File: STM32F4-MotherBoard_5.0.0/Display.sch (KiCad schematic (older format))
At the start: 4 parts

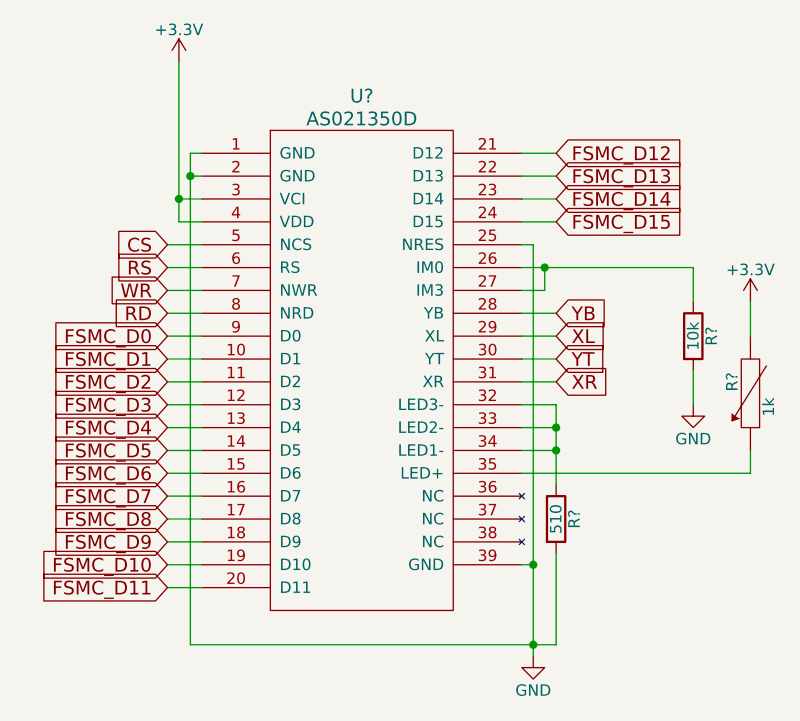
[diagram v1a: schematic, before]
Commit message: SDとCANの追加とラベルミス修正
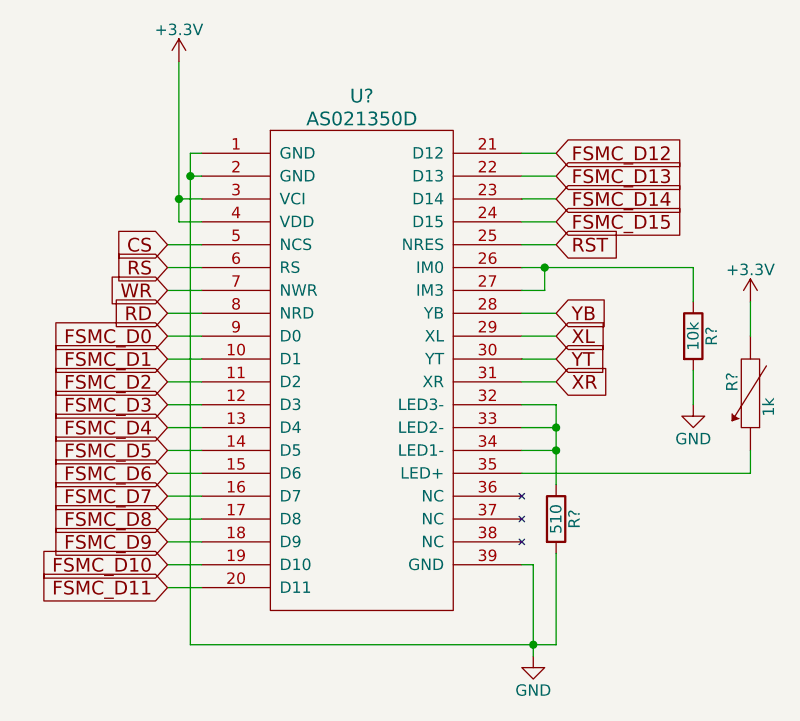
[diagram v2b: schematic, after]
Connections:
- net GND: no longer U?.25 (NRES)
- new net RST: U?.25 (NRES)
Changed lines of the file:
@@
 $Descr A4 11693 8268
 encoding utf-8
-Sheet 7 10
+Sheet 7 11
 Title ""
 Date ""
@@
 Wire Wire Line
 	6300 4750 6350 4750
-Wire Wire Line
-	6350 3350 6350 5150
 $Comp
 L R R?
@@
 Wire Wire Line
 	6300 3950 6450 3950
-Wire Wire Line
-	6300 3350 6350 3350
-Connection ~ 6350 4750
 Wire Wire Line
 	6300 3450 7050 3450
@@
 Text GLabel 4750 3350 0    60   Input ~ 0
 CS
+Wire Wire Line
+	6350 4750 6350 5150
+Text GLabel 6450 3350 2    60   Input ~ 0
+RST
+Wire Wire Line
+	6450 3350 6300 3350
 $EndSCHEMATC

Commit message: 回路図終わり
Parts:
- gave numbers to parts that had none: 4
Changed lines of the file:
@@
 $Descr A4 11693 8268
 encoding utf-8
-Sheet 7 11
+Sheet 7 12
 Title ""
 Date ""
@@
 $EndDescr
 $Comp
-L AS021350D U?
+L AS021350D U6
 U 1 1 589F41CD
 P 5600 2850
-F 0 "U?" H 5600 3000 60  0000 C CNN
+F 0 "U6" H 5600 3000 60  0000 C CNN
 F 1 "AS021350D" H 5600 2900 60  0000 C CNN
 F 2 "" H 5600 2850 60  0000 C CNN
@@
 $EndComp
 $Comp
-L +3.3V #PWR?
+L +3.3V #PWR059
 U 1 1 589F41F4
 P 4800 2550
-F 0 "#PWR?" H 4800 2400 50  0001 C CNN
+F 0 "#PWR059" H 4800 2400 50  0001 C CNN
 F 1 "+3.3V" H 4800 2690 50  0000 C CNN
 F 2 "" H 4800 2550 50  0000 C CNN
@@
 	6300 4750 6350 4750
 $Comp
-L R R?
+L R R31
 U 1 1 589F424B
 P 6450 4550
-F 0 "R?" V 6530 4550 50  0000 C CNN
+F 0 "R31" V 6530 4550 50  0000 C CNN
 F 1 "510" V 6450 4550 50  0000 C CNN
 F 2 "" V 6380 4550 50  0000 C CNN
@@
 Connection ~ 6350 5100
 $Comp
-L GND #PWR?
+L GND #PWR060
 U 1 1 589F4284
 P 6350 5150
-F 0 "#PWR?" H 6350 4900 50  0001 C CNN
+F 0 "#PWR060" H 6350 4900 50  0001 C CNN
 F 1 "GND" H 6350 5000 50  0000 C CNN
 F 2 "" H 6350 5150 50  0000 C CNN
@@
 	7300 4350 7300 4250
 $Comp
-L RVAR R?
+L RVAR R33
 U 1 1 589F433B
 P 7300 4000
-F 0 "R?" V 7380 3950 50  0000 C CNN
+F 0 "R33" V 7380 3950 50  0000 C CNN
 F 1 "1k" V 7220 4060 50  0000 C CNN
 F 2 "" H 7300 4000 50  0000 C CNN
@@
 	7300 3750 7300 3600
 $Comp
-L +3.3V #PWR?
+L +3.3V #PWR061
 U 1 1 589F43A6
 P 7300 3600
-F 0 "#PWR?" H 7300 3450 50  0001 C CNN
+F 0 "#PWR061" H 7300 3450 50  0001 C CNN
 F 1 "+3.3V" H 7300 3740 50  0000 C CNN
 F 2 "" H 7300 3600 50  0000 C CNN
@@
 Connection ~ 6400 3450
 $Comp
-L R R?
+L R R32
 U 1 1 589F454D
 P 7050 3750
-F 0 "R?" V 7130 3750 50  0000 C CNN
+F 0 "R32" V 7130 3750 50  0000 C CNN
 F 1 "10k" V 7050 3750 50  0000 C CNN
 F 2 "" V 6980 3750 50  0000 C CNN
@@
 $EndComp
 $Comp
-L GND #PWR?
+L GND #PWR062
 U 1 1 589F457E
 P 7050 4050
-F 0 "#PWR?" H 7050 3800 50  0001 C CNN
+F 0 "#PWR062" H 7050 3800 50  0001 C CNN
 F 1 "GND" H 7050 3900 50  0000 C CNN
 F 2 "" H 7050 4050 50  0000 C CNN

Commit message: 部品名変更
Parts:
- R31, R32, R33: footprint (none) -> robocon_pcb:SM0603_EXP0.5mm
- U6: footprint (none) -> mylib:ASO21350D
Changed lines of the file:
@@
 EESchema Schematic File Version 2
+LIBS:STM32F4-MotherBoard_5.0.0-rescue
 LIBS:power
 LIBS:device
@@
 F 0 "U6" H 5600 3000 60  0000 C CNN
 F 1 "AS021350D" H 5600 2900 60  0000 C CNN
-F 2 "" H 5600 2850 60  0000 C CNN
+F 2 "mylib:ASO21350D" H 5600 2850 60  0001 C CNN
 F 3 "" H 5600 2850 60  0000 C CNN
 	1    5600 2850
@@
 $EndComp
 $Comp
-L +3.3V #PWR059
+L +3.3V #PWR061
 U 1 1 589F41F4
 P 4800 2550
-F 0 "#PWR059" H 4800 2400 50  0001 C CNN
+F 0 "#PWR061" H 4800 2400 50  0001 C CNN
 F 1 "+3.3V" H 4800 2690 50  0000 C CNN
 F 2 "" H 4800 2550 50  0000 C CNN
@@
 F 0 "R31" V 6530 4550 50  0000 C CNN
 F 1 "510" V 6450 4550 50  0000 C CNN
-F 2 "" V 6380 4550 50  0000 C CNN
+F 2 "robocon_pcb:SM0603_EXP0.5mm" V 6380 4550 50  0001 C CNN
 F 3 "" H 6450 4550 50  0000 C CNN
 	1    6450 4550
@@
 Connection ~ 6350 5100
 $Comp
-L GND #PWR060
+L GND #PWR062
 U 1 1 589F4284
 P 6350 5150
-F 0 "#PWR060" H 6350 4900 50  0001 C CNN
+F 0 "#PWR062" H 6350 4900 50  0001 C CNN
 F 1 "GND" H 6350 5000 50  0000 C CNN
 F 2 "" H 6350 5150 50  0000 C CNN
@@
 F 0 "R33" V 7380 3950 50  0000 C CNN
 F 1 "1k" V 7220 4060 50  0000 C CNN
-F 2 "" H 7300 4000 50  0000 C CNN
+F 2 "robocon_pcb:SM0603_EXP0.5mm" H 7300 4000 50  0001 C CNN
 F 3 "" H 7300 4000 50  0000 C CNN
 	1    7300 4000
@@
 	7300 3750 7300 3600
 $Comp
-L +3.3V #PWR061
+L +3.3V #PWR063
 U 1 1 589F43A6
 P 7300 3600
-F 0 "#PWR061" H 7300 3450 50  0001 C CNN
+F 0 "#PWR063" H 7300 3450 50  0001 C CNN
 F 1 "+3.3V" H 7300 3740 50  0000 C CNN
 F 2 "" H 7300 3600 50  0000 C CNN
@@
 F 0 "R32" V 7130 3750 50  0000 C CNN
 F 1 "10k" V 7050 3750 50  0000 C CNN
-F 2 "" V 6980 3750 50  0000 C CNN
+F 2 "robocon_pcb:SM0603_EXP0.5mm" V 6980 3750 50  0001 C CNN
 F 3 "" H 7050 3750 50  0000 C CNN
 	1    7050 3750
@@
 $EndComp
 $Comp
-L GND #PWR062
+L GND #PWR064
 U 1 1 589F457E
 P 7050 4050
-F 0 "#PWR062" H 7050 3800 50  0001 C CNN
+F 0 "#PWR064" H 7050 3800 50  0001 C CNN
 F 1 "GND" H 7050 3900 50  0000 C CNN
 F 2 "" H 7050 4050 50  0000 C CNN
